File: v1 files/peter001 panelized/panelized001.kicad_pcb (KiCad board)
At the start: 2 copper layers, 79.8 x 94.7 mm, 15 parts

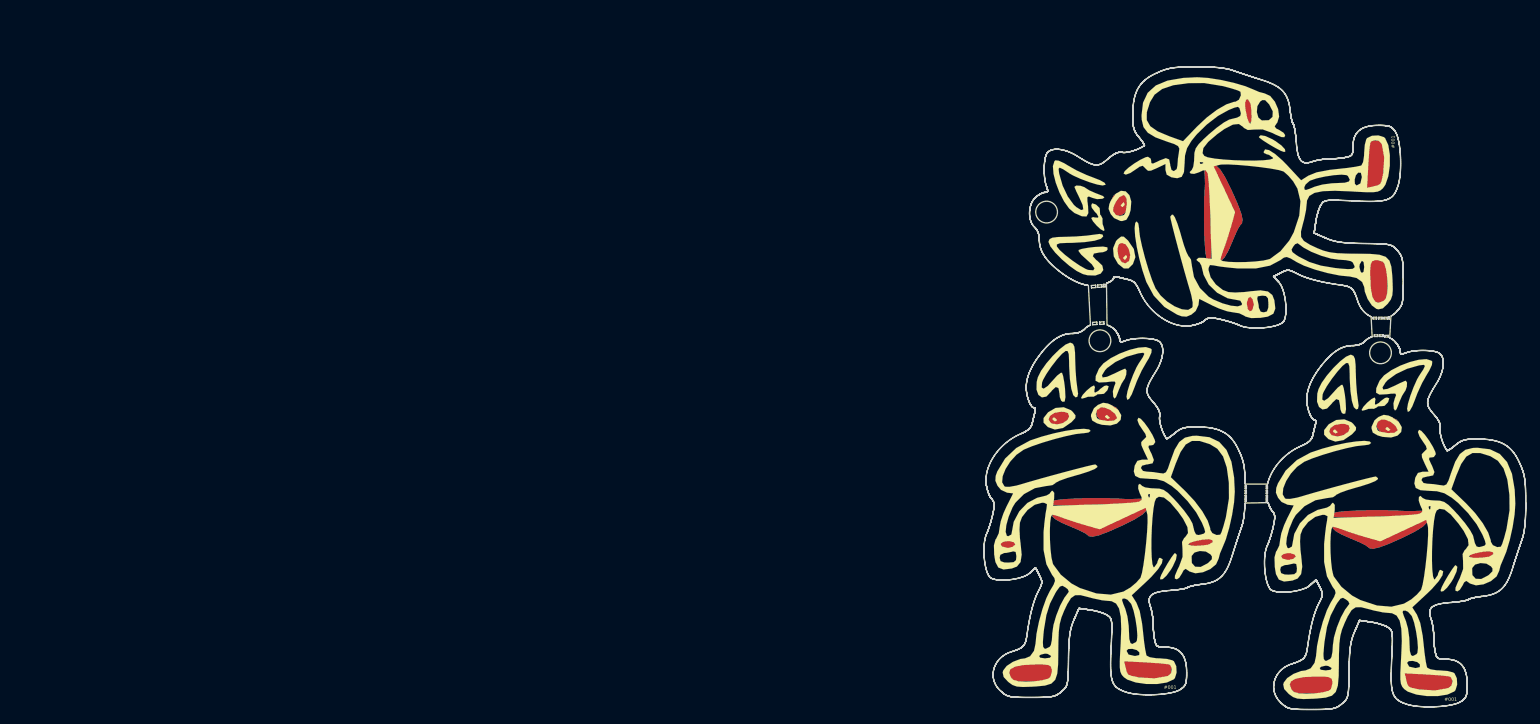
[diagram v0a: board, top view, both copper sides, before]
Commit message: panelized can fit 4 in 100x100mm
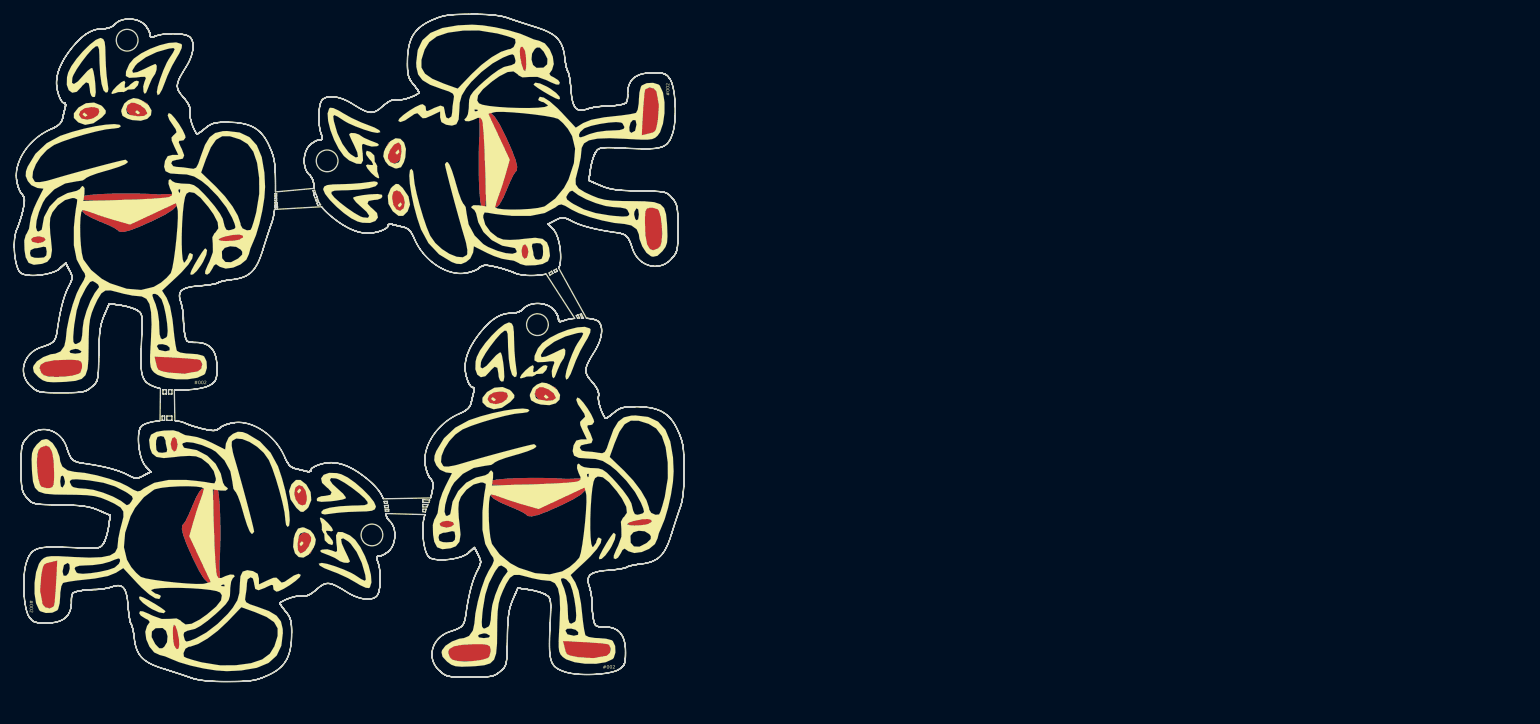
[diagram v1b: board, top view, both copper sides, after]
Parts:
- removed the G*** at (185.9, 108.8) (x2)
- removed the G*** at (202.2, 62.7) (x2)
- removed the G*** at (202.0, 62.7) (x2)
- removed the G*** at (185.9, 108.5) (x2)
- removed the G*** at (227.3, 110.6) (x2)
- removed the G*** at (227.3, 110.3) (x2)
- removed the REF** at (184.5, 83.1)
- removed the REF** at (225.8, 84.9)
- removed the REF** at (176.6, 64.2)
- added G***: LOGO, img:v3betterBSILK, F.Cu at (103.3, 105.8)
- added G***: LOGO, img:v5cucuBacking, F.Cu at (52.7, 113.4)
- added G***: LOGO, img:v5cucuFront, F.Cu at (52.7, 113.4)
- added G***: LOGO, img:v3better, F.Cu at (52.5, 113.4)
- added G***: LOGO, img:v3betterBSILK, F.Cu at (43.1, 63.9)
- added G***: LOGO, img:v5cucuBacking, F.Cu at (43.1, 63.6)
- added G***: LOGO, img:v5cucuFront, F.Cu at (43.1, 63.6)
- added G***: LOGO, img:v3better, F.Cu at (43.1, 63.9)
- added G***: LOGO, img:v5cucuBacking, F.Cu at (103.3, 105.5)
- added G***: LOGO, img:v5cucuFront, F.Cu at (103.3, 105.5)
- added G***: LOGO, img:v3better, F.Cu at (103.3, 105.8)
- added G***: LOGO, img:v3betterBSILK, F.Cu at (95.4, 55.0)
- added G***: LOGO, img:v5cucuBacking, F.Cu at (95.1, 55.0)
- added G***: LOGO, img:v5cucuFront, F.Cu at (95.1, 55.0)
- added G***: LOGO, img:v3better, F.Cu at (95.4, 55.0)
- added G***: LOGO, img:v3betterBSILK, F.Cu at (52.5, 113.4)
- added REF**: MountingHole_3.2mm_M3, MountingHole:MountingHole_3.2mm_M3, F.Cu at (101.6, 80.8)
- added REF**: MountingHole_3.2mm_M3, MountingHole:MountingHole_3.2mm_M3, F.Cu at (70.6, 56.6)
- added REF**: MountingHole_3.2mm_M3, MountingHole:MountingHole_3.2mm_M3, F.Cu at (77.2, 111.8)
- added REF**: MountingHole_3.2mm_M3, MountingHole:MountingHole_3.2mm_M3, F.Cu at (41.1, 38.9)
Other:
- board size 79.8 x 94.7 mm -> 98.7 x 98.3 mm
- board text added: "#002"
- board text removed: "#001"

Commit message: updated panelzing
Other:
- outline, holes or cut-outs redrawn
